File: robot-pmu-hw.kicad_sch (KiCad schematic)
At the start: 0 parts

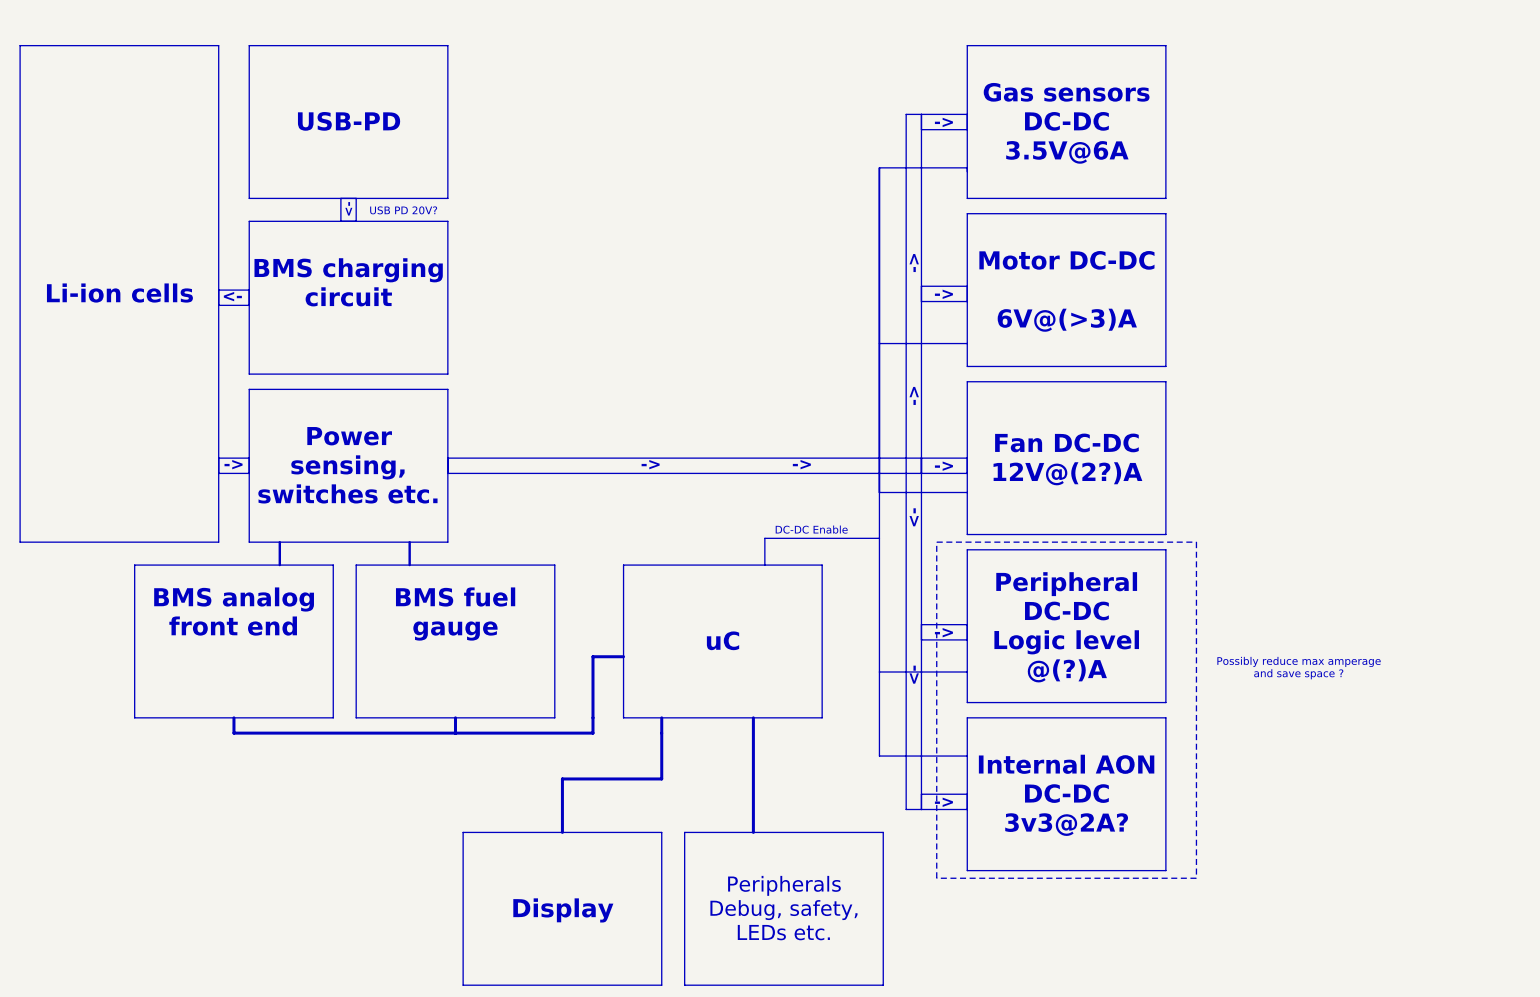
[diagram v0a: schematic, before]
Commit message: BMS symbol, protection FETs
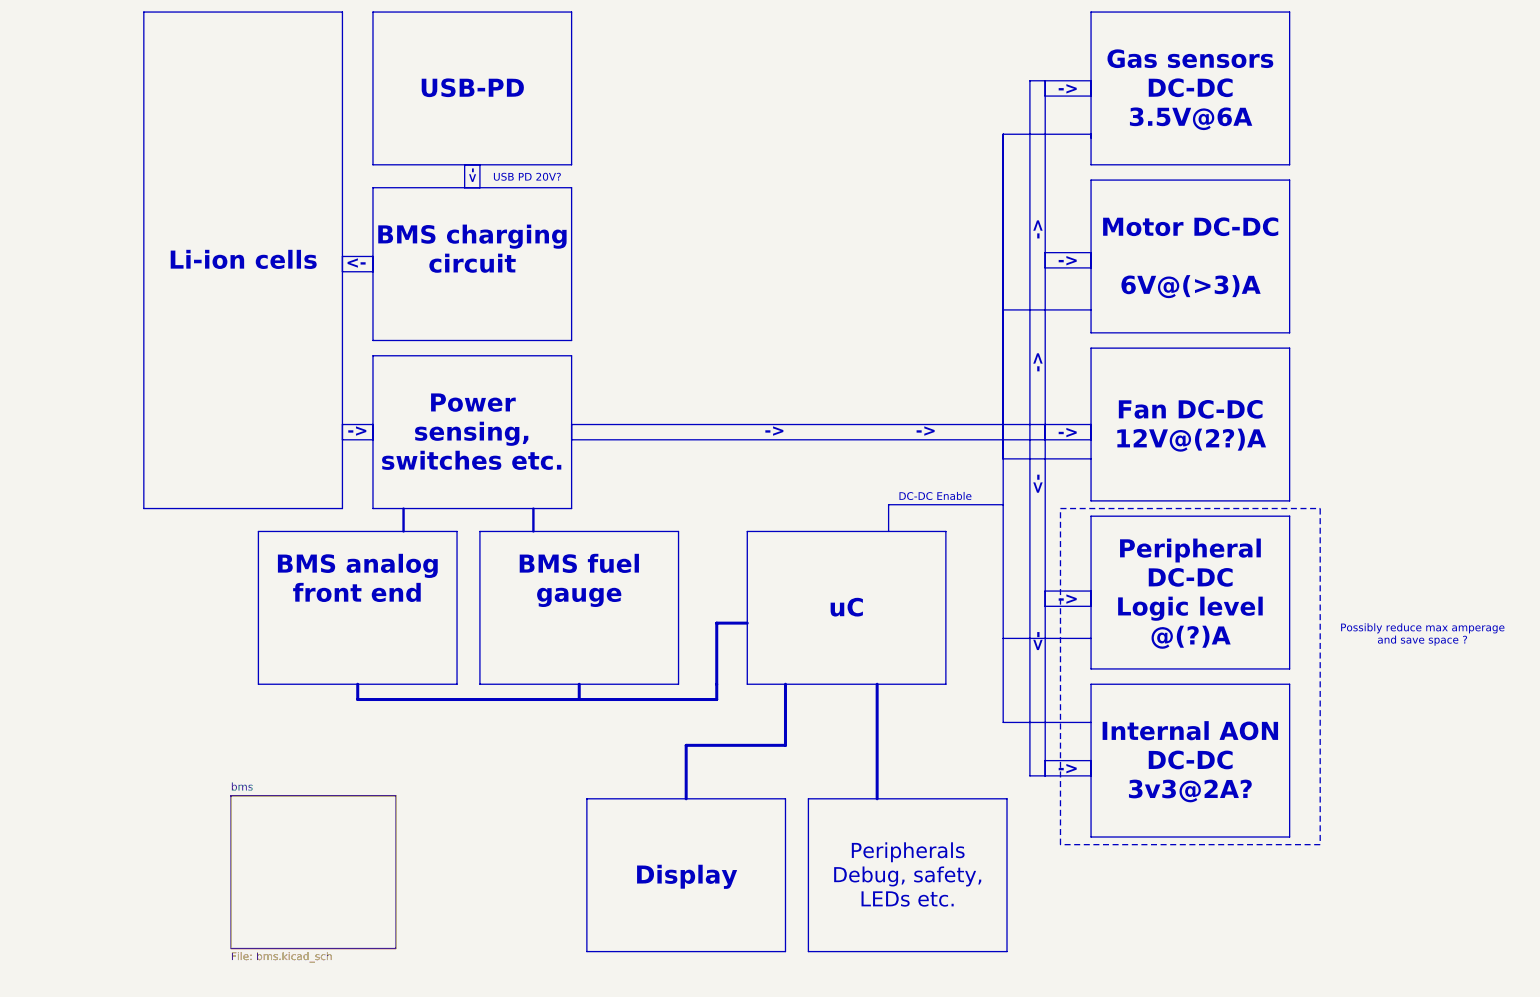
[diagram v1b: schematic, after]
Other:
- added sheet bms (bms.kicad_sch)
- title: (none) -> sniffer power managment unit

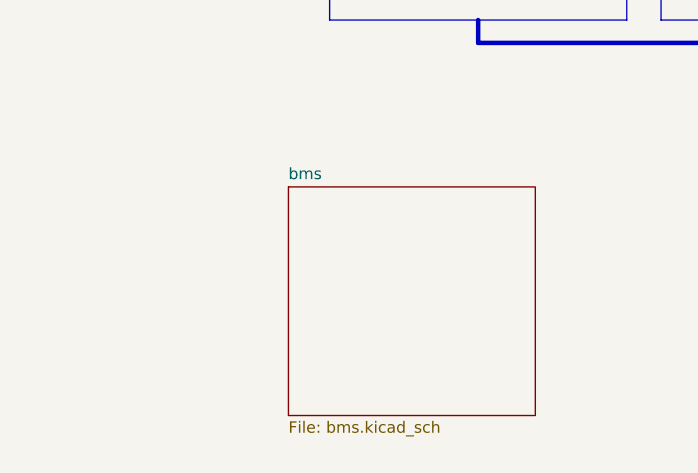
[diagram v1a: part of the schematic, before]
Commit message: Export footprints, symbols into a common library
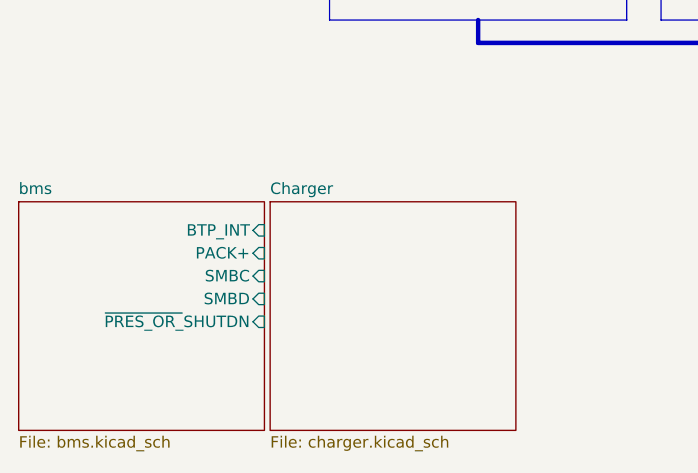
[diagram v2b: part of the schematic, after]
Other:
- added sheet Charger (charger.kicad_sch)
- sheet bms ports: added BTP_INT, PACK+, SMBC, SMBD, ~{PRES_OR_}SHUTDN; removed none
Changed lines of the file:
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@@
 	)
 	(sheet
-		(at 113.792 192.024)
-		(size 27.432 25.4)
+		(at 83.82 193.675)
+		(size 27.305 25.4)
 		(exclude_from_sim no)
 		(in_bom yes)
@@
 		)
 		(property "Sheetname" "bms"
-			(at 113.792 191.3124 0)
+			(at 83.82 192.9634 0)
 			(effects
 				(font
@@
 		)
 		(property "Sheetfile" "bms.kicad_sch"
-			(at 113.792 218.0086 0)
+			(at 83.82 219.6596 0)
+			(effects
+				(font
+					(size 1.27 1.27)
+				)
+				(justify left top)
+			)
+		)
+		(pin "BTP_INT" input
+			(at 111.125 196.85 0)
+			(effects
+				(font
+					(size 1.27 1.27)
+				)
+				(justify right)
+			)
+		)
+		(pin "PACK+" input
+			(at 111.125 199.39 0)
+			(effects
+				(font
+					(size 1.27 1.27)
+				)
+				(justify right)
+			)
+		)
+		(pin "SMBC" input
+			(at 111.125 201.93 0)
+			(effects
+				(font
+					(size 1.27 1.27)
+				)
+				(justify right)
+			)
+		)
+		(pin "SMBD" input
+			(at 111.125 204.47 0)
+			(effects
+				(font
+					(size 1.27 1.27)
+				)
+				(justify right)
+			)
+		)
+		(pin "~{PRES_OR_}SHUTDN" input
+			(at 111.125 207.01 0)
+			(effects
+				(font
+					(size 1.27 1.27)
+				)
+				(justify right)
+			)
+		)
+		(instances
+			(project "robot-pmu-hw"
+				(path "/ca7f4c4c-3c96-472a-b66f-ec124f8cf9b5"
+					(page "2")
+				)
+			)
+		)
+	)
+	(sheet
+		(at 111.76 193.675)
+		(size 27.305 25.4)
+		(exclude_from_sim no)
+		(in_bom yes)
+		(on_board yes)
+		(dnp no)
+		(fields_autoplaced yes)
+		(stroke
+			(width 0.1524)
+			(type solid)
+		)
+		(fill
+			(color 0 0 0 0.0000)
+		)
+		(property "Sheetname" "Charger"
+			(at 111.76 192.9634 0)
+			(effects
+				(font
+					(size 1.27 1.27)
+				)
+				(justify left bottom)
+			)
+		)
+		(property "Sheetfile" "charger.kicad_sch"
+			(at 111.76 219.6596 0)
 			(effects
 				(font
@@
 			(project "robot-pmu-hw"
 				(path "/ca7f4c4c-3c96-472a-b66f-ec124f8cf9b5"
-					(page "2")
+					(page "3")
 				)
 			)
